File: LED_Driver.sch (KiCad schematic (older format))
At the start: 6 parts, among them U7 AP5726

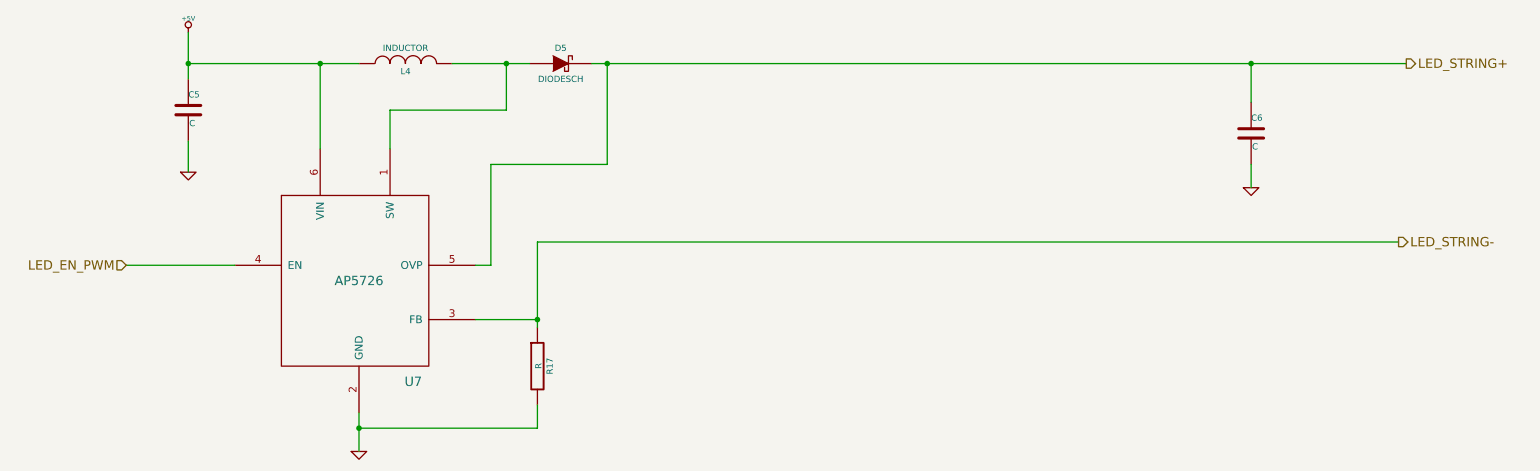
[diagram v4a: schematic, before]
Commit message: Associating the LED Module
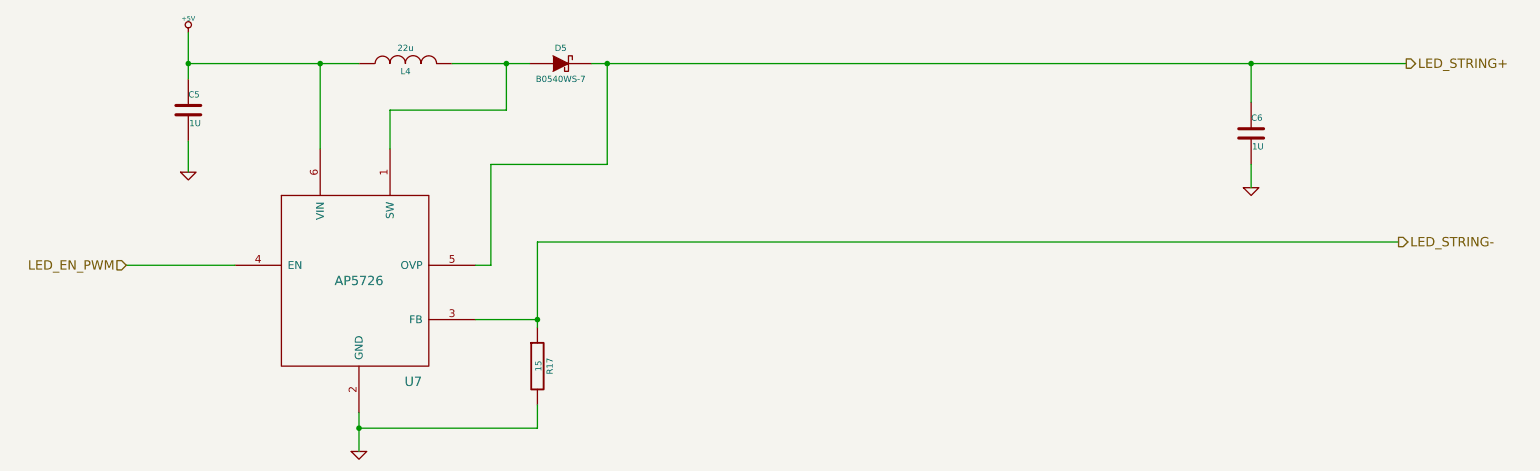
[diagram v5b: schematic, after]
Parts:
- C5, C6: value C -> 1U
- D5: value DIODESCH -> B0540WS-7
- L4: value INDUCTOR -> 22u; MFG Part Number (none) -> NR4012T220M
- R17: value R -> 15
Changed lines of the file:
@@
-EESchema Schematic File Version 2  date 10/22/2013 12:22:58 AM
+EESchema Schematic File Version 2  date 10/22/2013 8:47:41 PM
 LIBS:power
 LIBS:device
@@
 $Descr A4 11693 8268
 encoding utf-8
-Sheet 6 9
+Sheet 3 9
 Title ""
-Date "22 oct 2013"
+Date "23 oct 2013"
 Rev ""
 Comp ""
@@
 P 2550 1950
 F 0 "C5" H 2550 2050 40  0000 L CNN
-F 1 "C" H 2556 1865 40  0000 L CNN
+F 1 "1U" H 2556 1865 40  0000 L CNN
 F 2 "~" H 2588 1800 30  0000 C CNN
 F 3 "~" H 2550 1950 60  0000 C CNN
@@
 P 9400 2100
 F 0 "C6" H 9400 2200 40  0000 L CNN
-F 1 "C" H 9406 2015 40  0000 L CNN
+F 1 "1U" H 9406 2015 40  0000 L CNN
 F 2 "~" H 9438 1950 30  0000 C CNN
 F 3 "~" H 9400 2100 60  0000 C CNN
@@
 P 3950 1650
 F 0 "L4" V 3900 1650 40  0000 C CNN
-F 1 "INDUCTOR" V 4050 1650 40  0000 C CNN
+F 1 "22u" V 4050 1650 40  0000 C CNN
 F 2 "~" H 3950 1650 60  0000 C CNN
 F 3 "~" H 3950 1650 60  0000 C CNN
+F 4 "NR4012T220M" H 3950 1650 60  0001 C CNN "MFG Part Number"
 	1    3950 1650
 	0    -1   -1   0
@@
 P 4950 1650
 F 0 "D5" H 4950 1750 40  0000 C CNN
-F 1 "DIODESCH" H 4950 1550 40  0000 C CNN
+F 1 "B0540WS-7" H 4950 1550 40  0000 C CNN
 F 2 "~" H 4950 1650 60  0000 C CNN
 F 3 "~" H 4950 1650 60  0000 C CNN
@@
 P 4800 3600
 F 0 "R17" V 4880 3600 40  0000 C CNN
-F 1 "R" V 4807 3601 40  0000 C CNN
+F 1 "15" V 4807 3601 40  0000 C CNN
 F 2 "~" V 4730 3600 30  0000 C CNN
 F 3 "~" H 4800 3600 30  0000 C CNN

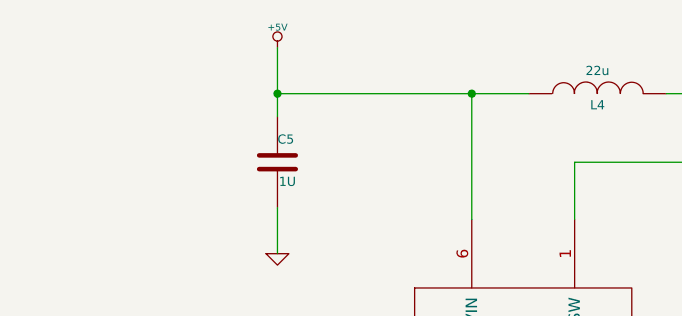
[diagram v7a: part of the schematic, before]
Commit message: More ground plane changes
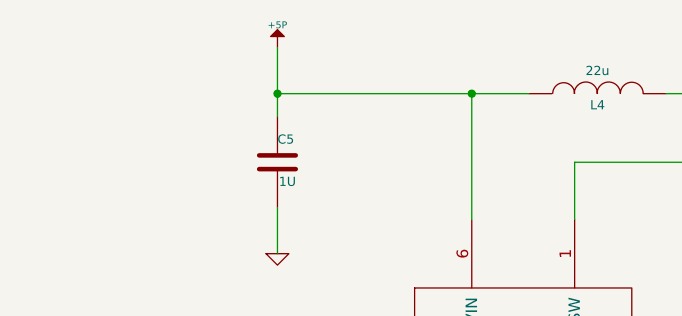
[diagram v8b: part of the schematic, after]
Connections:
- net +5V renamed +5P
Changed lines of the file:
@@
-EESchema Schematic File Version 2  date 10/27/2013 11:25:35 PM
+EESchema Schematic File Version 2  date 10/31/2013 9:00:44 PM
 LIBS:power
 LIBS:device
@@
 Sheet 3 9
 Title ""
-Date "28 oct 2013"
+Date "1 nov 2013"
 Rev ""
 Comp ""
@@
 	2150 2950 2850 2950
 $Comp
-L +5V #PWR016
-U 1 1 523F5D4A
-P 2550 1450
-F 0 "#PWR016" H 2550 1540 20  0001 C CNN
-F 1 "+5V" H 2550 1540 30  0000 C CNN
-F 2 "~" H 2550 1450 60  0000 C CNN
-F 3 "~" H 2550 1450 60  0000 C CNN
-	1    2550 1450
-	1    0    0    -1
-$EndComp
-$Comp
-L GND #PWR017
+L GND #PWR20
 U 1 1 523F5D68
 P 2550 2350
-F 0 "#PWR017" H 2550 2350 30  0001 C CNN
+F 0 "#PWR20" H 2550 2350 30  0001 C CNN
 F 1 "GND" H 2550 2280 30  0001 C CNN
 F 2 "~" H 2550 2350 60  0000 C CNN
@@
 $EndComp
 $Comp
-L GND #PWR018
+L GND #PWR21
 U 1 1 523F5D75
 P 3650 4150
-F 0 "#PWR018" H 3650 4150 30  0001 C CNN
+F 0 "#PWR21" H 3650 4150 30  0001 C CNN
 F 1 "GND" H 3650 4080 30  0001 C CNN
 F 2 "~" H 3650 4150 60  0000 C CNN
@@
 	9400 1650 9400 1900
 $Comp
-L GND #PWR019
+L GND #PWR22
 U 1 1 523F5E22
 P 9400 2450
-F 0 "#PWR019" H 9400 2450 30  0001 C CNN
+F 0 "#PWR22" H 9400 2450 30  0001 C CNN
 F 1 "GND" H 9400 2380 30  0001 C CNN
 F 2 "~" H 9400 2450 60  0000 C CNN
@@
 Text HLabel 10350 2800 2    60   Output ~ 0
 LED_STRING-
+$Comp
+L +5P #PWR19
+U 1 1 527304B1
+P 2550 1450
+F 0 "#PWR19" H 2550 1580 20  0001 C CNN
+F 1 "+5P" H 2550 1550 30  0000 C CNN
+F 2 "~" H 2550 1450 60  0000 C CNN
+F 3 "~" H 2550 1450 60  0000 C CNN
+	1    2550 1450
+	1    0    0    -1
+$EndComp
 $EndSCHEMATC
